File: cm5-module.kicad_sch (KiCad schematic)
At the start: 1 part

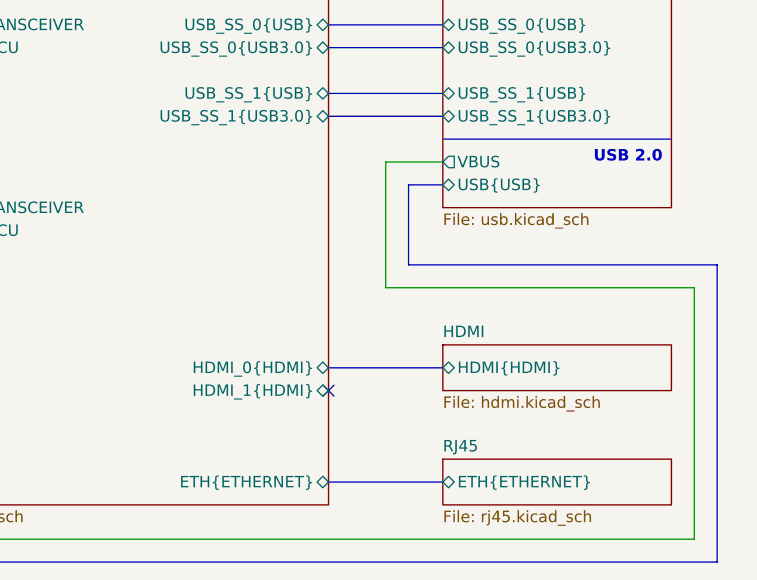
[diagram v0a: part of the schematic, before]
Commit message: [#3] Add GND pours on top and bottom
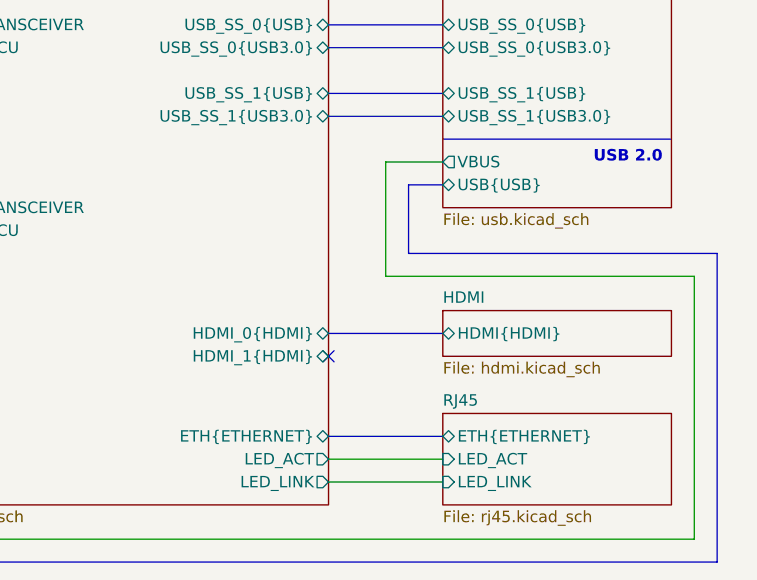
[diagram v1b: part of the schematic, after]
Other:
- sheet CM5 ports: added LED_ACT, LED_LINK; removed none
- sheet RJ45 ports: added LED_ACT, LED_LINK; removed none
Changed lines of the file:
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@@
 	)
 	(no_connect
-		(at 214.63 139.7)
+		(at 214.63 135.89)
 	)
 	(no_connect
@@
 		)
 	)
+	(wire
+		(pts
+			(xy 214.63 147.32) (xy 227.33 147.32)
+		)
+		(stroke
+			(width 0)
+			(type default)
+		)
+	)
 	(bus
 		(pts
@@
 	(wire
 		(pts
-			(xy 220.98 114.3) (xy 220.98 128.27)
+			(xy 220.98 114.3) (xy 220.98 127)
 		)
 		(stroke
@@
 	(bus
 		(pts
-			(xy 257.81 125.73) (xy 223.52 125.73)
+			(xy 257.81 124.46) (xy 223.52 124.46)
 		)
 		(stroke
@@
 	(bus
 		(pts
-			(xy 223.52 125.73) (xy 223.52 116.84)
+			(xy 223.52 124.46) (xy 223.52 116.84)
 		)
 		(stroke
@@
 		)
 	)
-	(bus
-		(pts
-			(xy 214.63 149.86) (xy 227.33 149.86)
-		)
-		(stroke
-			(width 0)
-			(type default)
-		)
-	)
 	(wire
 		(pts
@@
 	(bus
 		(pts
-			(xy 257.81 158.75) (xy 257.81 125.73)
-		)
-		(stroke
-			(width 0)
-			(type default)
-		)
-	)
-	(bus
-		(pts
-			(xy 214.63 137.16) (xy 227.33 137.16)
+			(xy 257.81 158.75) (xy 257.81 124.46)
+		)
+		(stroke
+			(width 0)
+			(type default)
+		)
+	)
+	(bus
+		(pts
+			(xy 214.63 133.35) (xy 227.33 133.35)
 		)
 		(stroke
@@
 	(wire
 		(pts
-			(xy 255.27 128.27) (xy 255.27 156.21)
+			(xy 255.27 127) (xy 255.27 156.21)
 		)
 		(stroke
@@
 	(wire
 		(pts
-			(xy 220.98 128.27) (xy 255.27 128.27)
+			(xy 220.98 127) (xy 255.27 127)
 		)
 		(stroke
@@
 		(pts
 			(xy 102.87 101.6) (xy 163.83 101.6)
+		)
+		(stroke
+			(width 0)
+			(type default)
+		)
+	)
+	(wire
+		(pts
+			(xy 214.63 149.86) (xy 227.33 149.86)
+		)
+		(stroke
+			(width 0)
+			(type default)
+		)
+	)
+	(bus
+		(pts
+			(xy 214.63 144.78) (xy 227.33 144.78)
 		)
 		(stroke
@@
 	)
 	(sheet
-		(at 227.33 134.62)
+		(at 227.33 130.81)
 		(size 25.4 5.08)
 		(exclude_from_sim no)
@@
 		)
 		(property "Sheetname" "HDMI"
-			(at 227.33 133.9084 0)
+			(at 227.33 130.0984 0)
 			(effects
 				(font
@@
 		)
 		(property "Sheetfile" "hdmi.kicad_sch"
-			(at 227.33 140.2846 0)
+			(at 227.33 136.4746 0)
 			(effects
 				(font
@@
 		)
 		(pin "HDMI{HDMI}" bidirectional
-			(at 227.33 137.16 180)
+			(at 227.33 133.35 180)
 			(effects
 				(font
@@
 	)
 	(sheet
-		(at 227.33 147.32)
-		(size 25.4 5.08)
+		(at 227.33 142.24)
+		(size 25.4 10.16)
 		(exclude_from_sim no)
 		(in_bom yes)
@@
 		)
 		(property "Sheetname" "RJ45"
-			(at 227.33 146.6084 0)
+			(at 227.33 141.5284 0)
 			(effects
 				(font
@@
 		)
 		(pin "ETH{ETHERNET}" bidirectional
+			(at 227.33 144.78 180)
+			(effects
+				(font
+					(size 1.27 1.27)
+				)
+				(justify left)
+			)
+		)
+		(pin "LED_ACT" input
+			(at 227.33 147.32 180)
+			(effects
+				(font
+					(size 1.27 1.27)
+				)
+				(justify left)
+			)
+		)
+		(pin "LED_LINK" input
 			(at 227.33 149.86 180)
 			(effects
@@
 		)
 		(pin "ETH{ETHERNET}" bidirectional
-			(at 214.63 149.86 0)
+			(at 214.63 144.78 0)
 			(effects
 				(font
@@
 		)
 		(pin "HDMI_1{HDMI}" bidirectional
-			(at 214.63 139.7 0)
+			(at 214.63 135.89 0)
 			(effects
 				(font
@@
 		)
 		(pin "HDMI_0{HDMI}" bidirectional
-			(at 214.63 137.16 0)
+			(at 214.63 133.35 0)
 			(effects
 				(font
@@
 			(effects
 				(font
+					(size 1.27 1.27)
+				)
+				(justify right)
+			)
+		)
+		(pin "LED_ACT" output
+			(at 214.63 147.32 0)
+			(effects
+				(font
+					(size 1.27 1.27)
+				)
+				(justify right)
+			)
+		)
+		(pin "LED_LINK" output
+			(at 214.63 149.86 0)
+			(effects
+				(font
